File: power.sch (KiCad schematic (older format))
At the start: 11 parts

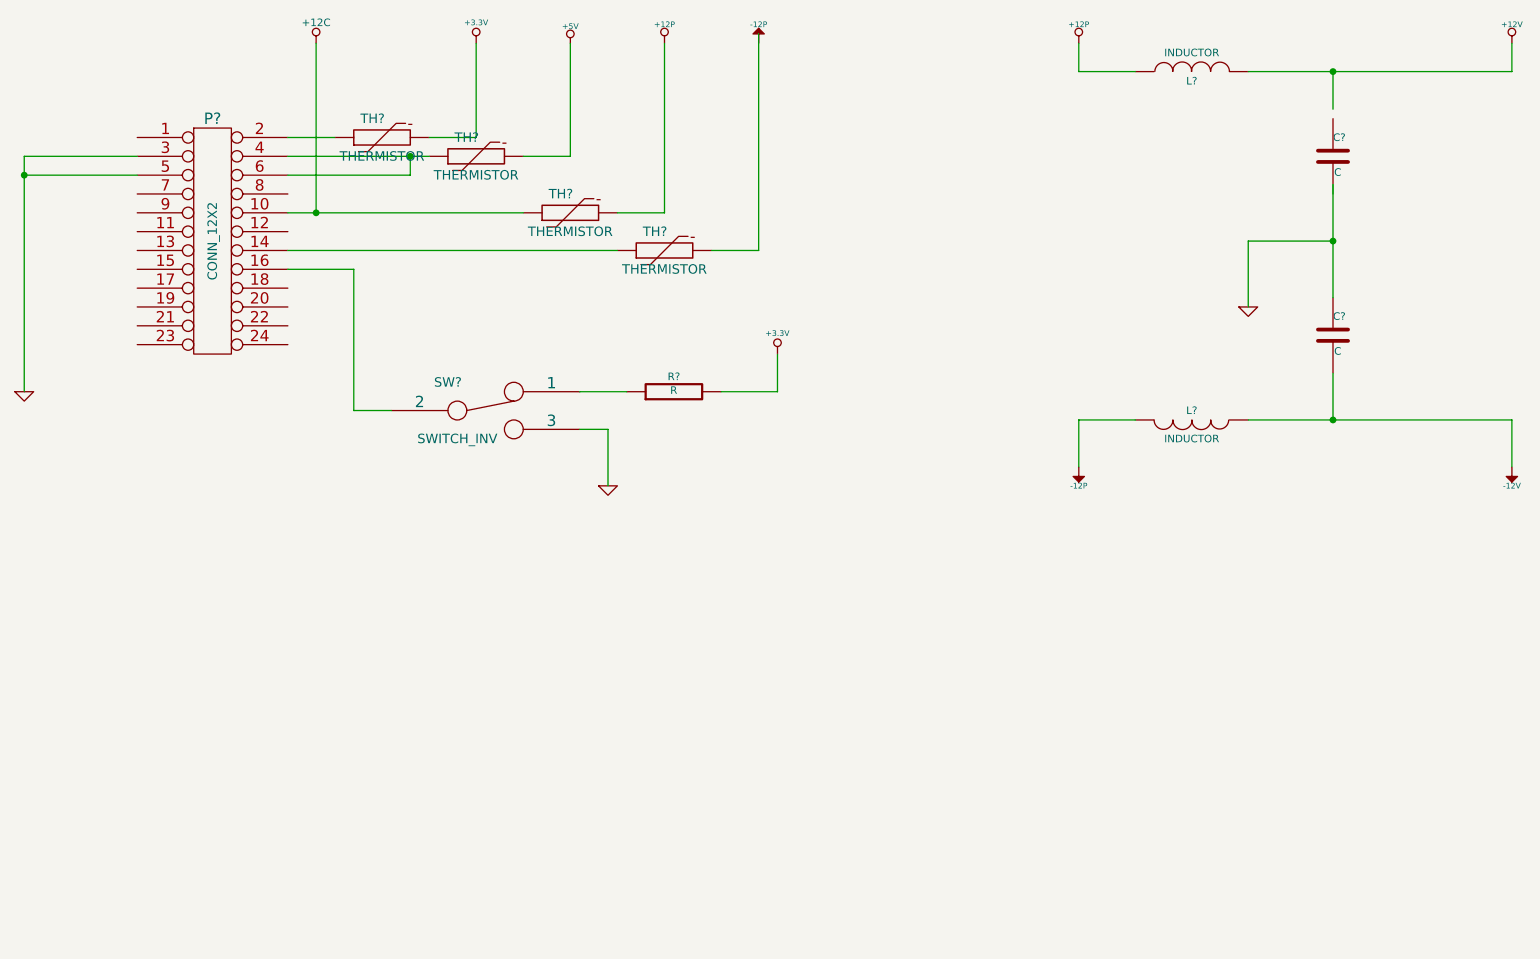
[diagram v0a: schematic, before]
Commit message: Module 3 Unit 15
Choosing Components For The Power Control, Conditioning, Monitoring
Module
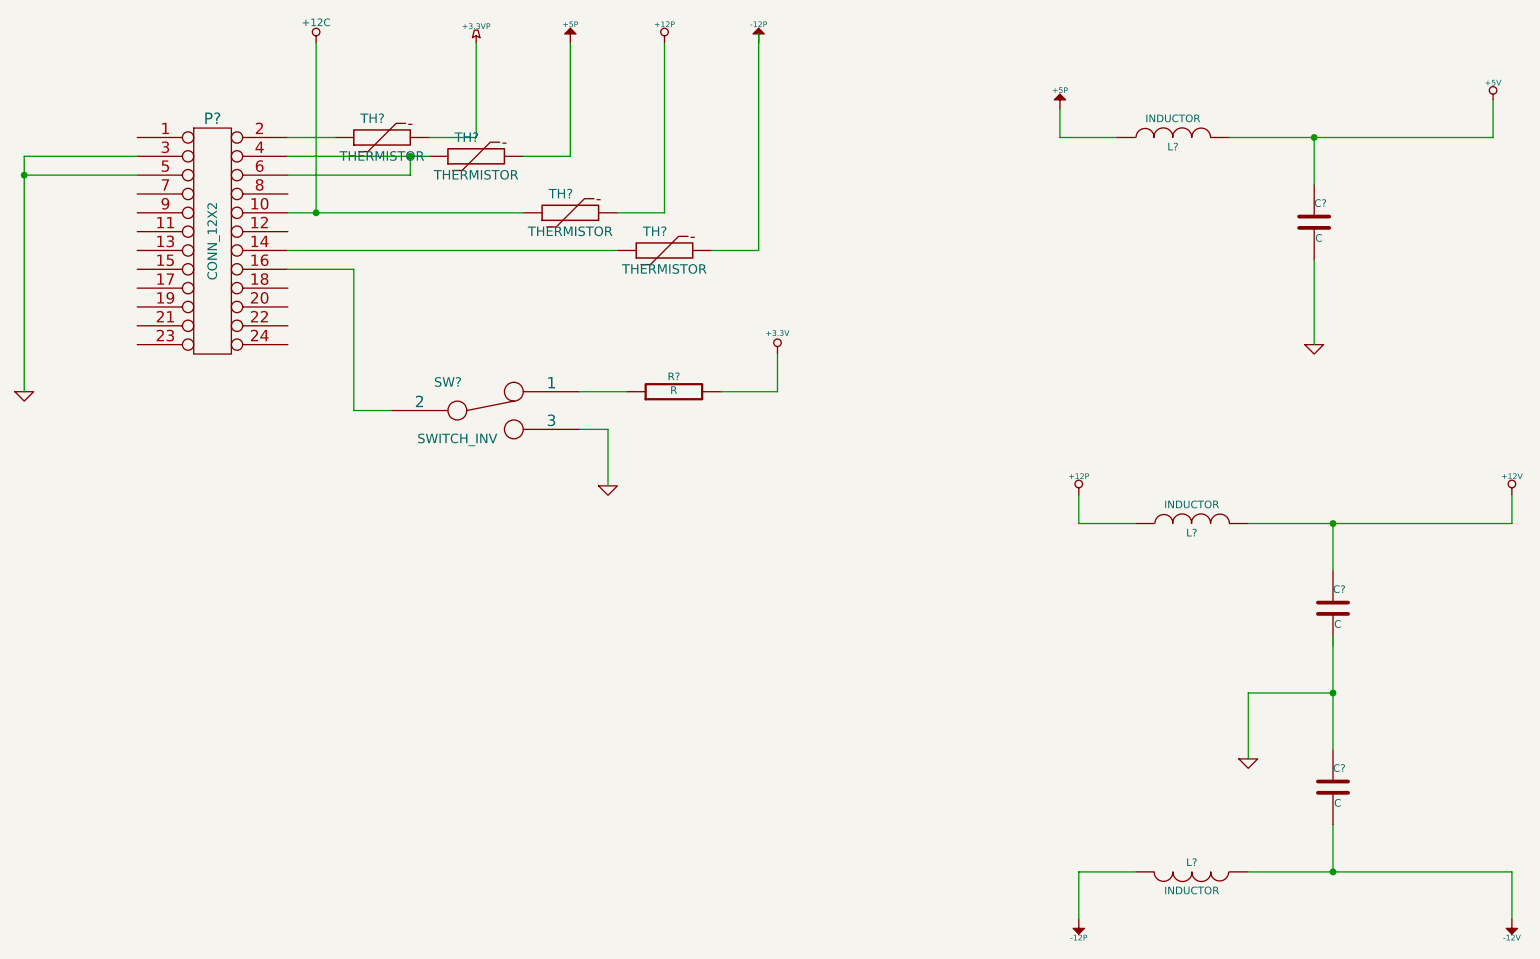
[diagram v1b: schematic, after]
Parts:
- added C?: C, ~, symbol C
- added L?: INDUCTOR, ~, symbol INDUCTOR
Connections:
- net labels added: +3.3VP, +5P
- wire segments 39 -> 45
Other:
- moved on the sheet: C?, L?
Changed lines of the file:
@@
 Sheet 4 9
 Title ""
-Date "16 feb 2014"
+Date "22 feb 2014"
 Rev ""
 Comp ""
@@
 	1    0    0    -1
 $EndComp
-$Comp
-L +3.3V #PWR014
-U 1 1 52F953A2
-P 3200 700
-F 0 "#PWR014" H 3200 660 30  0001 C CNN
-F 1 "+3.3V" H 3200 810 30  0000 C CNN
-F 2 "" H 3200 700 60  0000 C CNN
-F 3 "" H 3200 700 60  0000 C CNN
-	1    3200 700
-	1    0    0    -1
-$EndComp
-$Comp
-L +5V #PWR015
-U 1 1 52F953BC
-P 3700 700
-F 0 "#PWR015" H 3700 790 20  0001 C CNN
-F 1 "+5V" H 3700 790 30  0000 C CNN
-F 2 "" H 3700 700 60  0000 C CNN
-F 3 "" H 3700 700 60  0000 C CNN
-	1    3700 700
-	1    0    0    -1
-$EndComp
 Wire Wire Line
 	1400 1300 800  1300
@@
 L +12P #PWR020
 U 1 1 52F95C8B
-P 6400 700
-F 0 "#PWR020" H 6400 670 30  0001 C CNN
-F 1 "+12P" H 6400 800 30  0000 C CNN
-F 2 "" H 6400 700 60  0000 C CNN
-F 3 "" H 6400 700 60  0000 C CNN
-	1    6400 700
+P 6400 3100
+F 0 "#PWR020" H 6400 3070 30  0001 C CNN
+F 1 "+12P" H 6400 3200 30  0000 C CNN
+F 2 "" H 6400 3100 60  0000 C CNN
+F 3 "" H 6400 3100 60  0000 C CNN
+	1    6400 3100
 	1    0    0    -1
 $EndComp
@@
 L -12P #PWR021
 U 1 1 52F95C91
-P 6400 2950
-F 0 "#PWR021" H 6400 3080 20  0001 C CNN
-F 1 "-12P" H 6400 3050 30  0000 C CNN
-F 2 "" H 6400 2950 60  0000 C CNN
-F 3 "" H 6400 2950 60  0000 C CNN
-	1    6400 2950
+P 6400 5350
+F 0 "#PWR021" H 6400 5480 20  0001 C CNN
+F 1 "-12P" H 6400 5450 30  0000 C CNN
+F 2 "" H 6400 5350 60  0000 C CNN
+F 3 "" H 6400 5350 60  0000 C CNN
+	1    6400 5350
 	-1   0    0    1
 $EndComp
@@
 L GND #PWR022
 U 1 1 52F95C97
-P 7300 2100
-F 0 "#PWR022" H 7300 2100 30  0001 C CNN
-F 1 "GND" H 7300 2030 30  0001 C CNN
-F 2 "" H 7300 2100 60  0000 C CNN
-F 3 "" H 7300 2100 60  0000 C CNN
-	1    7300 2100
+P 7300 4500
+F 0 "#PWR022" H 7300 4500 30  0001 C CNN
+F 1 "GND" H 7300 4430 30  0001 C CNN
+F 2 "" H 7300 4500 60  0000 C CNN
+F 3 "" H 7300 4500 60  0000 C CNN
+	1    7300 4500
 	1    0    0    -1
 $EndComp
@@
 L INDUCTOR L?
 U 1 1 52F95CA9
-P 7000 850
-F 0 "L?" V 6950 850 40  0000 C CNN
-F 1 "INDUCTOR" V 7100 850 40  0000 C CNN
-F 2 "~" H 7000 850 60  0000 C CNN
-F 3 "~" H 7000 850 60  0000 C CNN
-	1    7000 850
+P 7000 3250
+F 0 "L?" V 6950 3250 40  0000 C CNN
+F 1 "INDUCTOR" V 7100 3250 40  0000 C CNN
+F 2 "~" H 7000 3250 60  0000 C CNN
+F 3 "~" H 7000 3250 60  0000 C CNN
+	1    7000 3250
 	0    -1   -1   0
 $EndComp
@@
 L INDUCTOR L?
 U 1 1 52F95CB6
-P 7000 2700
-F 0 "L?" V 6950 2700 40  0000 C CNN
-F 1 "INDUCTOR" V 7100 2700 40  0000 C CNN
-F 2 "~" H 7000 2700 60  0000 C CNN
-F 3 "~" H 7000 2700 60  0000 C CNN
-	1    7000 2700
+P 7000 5100
+F 0 "L?" V 6950 5100 40  0000 C CNN
+F 1 "INDUCTOR" V 7100 5100 40  0000 C CNN
+F 2 "~" H 7000 5100 60  0000 C CNN
+F 3 "~" H 7000 5100 60  0000 C CNN
+	1    7000 5100
 	0    1    1    0
 $EndComp
@@
 L C C?
 U 1 1 52F95CC8
-P 7750 1300
-F 0 "C?" H 7750 1400 40  0000 L CNN
-F 1 "C" H 7756 1215 40  0000 L CNN
-F 2 "~" H 7788 1150 30  0000 C CNN
-F 3 "~" H 7750 1300 60  0000 C CNN
-	1    7750 1300
+P 7750 3700
+F 0 "C?" H 7750 3800 40  0000 L CNN
+F 1 "C" H 7756 3615 40  0000 L CNN
+F 2 "~" H 7788 3550 30  0000 C CNN
+F 3 "~" H 7750 3700 60  0000 C CNN
+	1    7750 3700
 	1    0    0    -1
 $EndComp
@@
 L C C?
 U 1 1 52F95CD5
-P 7750 2250
-F 0 "C?" H 7750 2350 40  0000 L CNN
-F 1 "C" H 7756 2165 40  0000 L CNN
-F 2 "~" H 7788 2100 30  0000 C CNN
-F 3 "~" H 7750 2250 60  0000 C CNN
-	1    7750 2250
-	1    0    0    -1
-$EndComp
-Wire Wire Line
-	7300 2700 8700 2700
-Wire Wire Line
-	7750 2700 7750 2450
-Wire Wire Line
-	7750 2050 7750 1450
-Wire Wire Line
-	7750 1050 7750 850
-Wire Wire Line
-	7300 850  8700 850
-Wire Wire Line
-	6400 700  6400 850
-Wire Wire Line
-	6400 850  6700 850
-Wire Wire Line
-	6400 2950 6400 2700
-Wire Wire Line
-	6400 2700 6700 2700
-Wire Wire Line
-	7300 2100 7300 1750
-Wire Wire Line
-	7300 1750 7750 1750
-Connection ~ 7750 1750
+P 7750 4650
+F 0 "C?" H 7750 4750 40  0000 L CNN
+F 1 "C" H 7756 4565 40  0000 L CNN
+F 2 "~" H 7788 4500 30  0000 C CNN
+F 3 "~" H 7750 4650 60  0000 C CNN
+	1    7750 4650
+	1    0    0    -1
+$EndComp
+Wire Wire Line
+	7300 5100 8700 5100
+Wire Wire Line
+	7750 5100 7750 4850
+Wire Wire Line
+	7750 4450 7750 3850
+Wire Wire Line
+	7300 3250 8700 3250
+Wire Wire Line
+	6400 3100 6400 3250
+Wire Wire Line
+	6400 3250 6700 3250
+Wire Wire Line
+	6400 5350 6400 5100
+Wire Wire Line
+	6400 5100 6700 5100
+Wire Wire Line
+	7300 4500 7300 4150
+Wire Wire Line
+	7300 4150 7750 4150
+Connection ~ 7750 4150
 $Comp
 L -12V #PWR023
 U 1 1 52F95E22
-P 8700 2950
-F 0 "#PWR023" H 8700 3080 20  0001 C CNN
-F 1 "-12V" H 8700 3050 30  0000 C CNN
-F 2 "" H 8700 2950 60  0000 C CNN
-F 3 "" H 8700 2950 60  0000 C CNN
-	1    8700 2950
+P 8700 5350
+F 0 "#PWR023" H 8700 5480 20  0001 C CNN
+F 1 "-12V" H 8700 5450 30  0000 C CNN
+F 2 "" H 8700 5350 60  0000 C CNN
+F 3 "" H 8700 5350 60  0000 C CNN
+	1    8700 5350
 	-1   0    0    1
 $EndComp
@@
 L +12V #PWR024
 U 1 1 52F95E45
-P 8700 700
-F 0 "#PWR024" H 8700 650 20  0001 C CNN
-F 1 "+12V" H 8700 800 30  0000 C CNN
-F 2 "" H 8700 700 60  0000 C CNN
-F 3 "" H 8700 700 60  0000 C CNN
-	1    8700 700
-	1    0    0    -1
-$EndComp
-Wire Wire Line
-	8700 850  8700 700
-Connection ~ 7750 850
-Wire Wire Line
-	8700 2700 8700 2950
-Connection ~ 7750 2700
+P 8700 3100
+F 0 "#PWR024" H 8700 3050 20  0001 C CNN
+F 1 "+12V" H 8700 3200 30  0000 C CNN
+F 2 "" H 8700 3100 60  0000 C CNN
+F 3 "" H 8700 3100 60  0000 C CNN
+	1    8700 3100
+	1    0    0    -1
+$EndComp
+Wire Wire Line
+	8700 3250 8700 3100
+Connection ~ 7750 3250
+Wire Wire Line
+	8700 5100 8700 5350
+Connection ~ 7750 5100
 $Comp
 L +12C #PWR?
@@
 	0    -1   -1   0
 $EndComp
+$Comp
+L GND #PWR?
+U 1 1 5308CDC3
+P 7650 2300
+F 0 "#PWR?" H 7650 2300 30  0001 C CNN
+F 1 "GND" H 7650 2230 30  0001 C CNN
+F 2 "" H 7650 2300 60  0000 C CNN
+F 3 "" H 7650 2300 60  0000 C CNN
+	1    7650 2300
+	1    0    0    -1
+$EndComp
+$Comp
+L INDUCTOR L?
+U 1 1 5308CDC9
+P 6900 1200
+F 0 "L?" V 6850 1200 40  0000 C CNN
+F 1 "INDUCTOR" V 7000 1200 40  0000 C CNN
+F 2 "~" H 6900 1200 60  0000 C CNN
+F 3 "~" H 6900 1200 60  0000 C CNN
+	1    6900 1200
+	0    -1   -1   0
+$EndComp
+$Comp
+L C C?
+U 1 1 5308CDCF
+P 7650 1650
+F 0 "C?" H 7650 1750 40  0000 L CNN
+F 1 "C" H 7656 1565 40  0000 L CNN
+F 2 "~" H 7688 1500 30  0000 C CNN
+F 3 "~" H 7650 1650 60  0000 C CNN
+	1    7650 1650
+	1    0    0    -1
+$EndComp
+Wire Wire Line
+	7200 1200 8600 1200
+Wire Wire Line
+	6300 1050 6300 1200
+Wire Wire Line
+	6300 1200 6600 1200
+Wire Wire Line
+	7750 3250 7750 3500
+Wire Wire Line
+	7650 1200 7650 1450
+Connection ~ 7650 1200
+$Comp
+L +5P #PWR?
+U 1 1 5308CE8A
+P 3700 700
+F 0 "#PWR?" H 3700 830 20  0001 C CNN
+F 1 "+5P" H 3700 800 30  0000 C CNN
+F 2 "" H 3700 700 60  0000 C CNN
+F 3 "" H 3700 700 60  0000 C CNN
+	1    3700 700
+	1    0    0    -1
+$EndComp
+$Comp
+L +3.3VP #PWR?
+U 1 1 5308CEA3
+P 3200 700
+F 0 "#PWR?" H 3250 730 20  0001 C CNN
+F 1 "+3.3VP" H 3200 790 30  0000 C CNN
+F 2 "" H 3200 700 60  0000 C CNN
+F 3 "" H 3200 700 60  0000 C CNN
+	1    3200 700
+	1    0    0    -1
+$EndComp
+$Comp
+L +5P #PWR?
+U 1 1 5308CEB0
+P 6300 1050
+F 0 "#PWR?" H 6300 1180 20  0001 C CNN
+F 1 "+5P" H 6300 1150 30  0000 C CNN
+F 2 "" H 6300 1050 60  0000 C CNN
+F 3 "" H 6300 1050 60  0000 C CNN
+	1    6300 1050
+	1    0    0    -1
+$EndComp
+$Comp
+L +5V #PWR?
+U 1 1 5308CEB8
+P 8600 1000
+F 0 "#PWR?" H 8600 1090 20  0001 C CNN
+F 1 "+5V" H 8600 1090 30  0000 C CNN
+F 2 "" H 8600 1000 60  0000 C CNN
+F 3 "" H 8600 1000 60  0000 C CNN
+	1    8600 1000
+	1    0    0    -1
+$EndComp
+Wire Wire Line
+	8600 1200 8600 1000
+Wire Wire Line
+	7650 1850 7650 2300
 $EndSCHEMATC
